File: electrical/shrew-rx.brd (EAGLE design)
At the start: 14 x 14 mm, 28 parts, among them U1 ESP32-PICO-D4, U2 SX1280IMLTRT, Y1 52MHz TCXO

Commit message: wip for rx
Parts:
- C12: value 470n -> DNP
- C17: value 100n -> 470n
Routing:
- net GND: track 27.7 -> 35.9 mm

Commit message: rx mfg file trial run
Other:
- board size 14 x 14 mm -> 15.5 x 15 mm
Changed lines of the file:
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@@
 <setting verticaltext="up"/>
 </settings>
-<grid distance="0.1" unitdist="mm" unit="mm" style="dots" multiple="10" display="no" altdistance="0.01" altunitdist="mm" altunit="mm"/>
+<grid distance="0.1" unitdist="mm" unit="mm" style="dots" multiple="10" display="yes" altdistance="0.01" altunitdist="mm" altunit="mm"/>
 <layers>
 <layer number="1" name="Top" color="4" fill="1" visible="yes" active="yes"/>
@@
 <layer number="21" name="tPlace" color="7" fill="1" visible="yes" active="yes"/>
 <layer number="22" name="bPlace" color="7" fill="1" visible="yes" active="yes"/>
-<layer number="23" name="tOrigins" color="15" fill="1" visible="yes" active="yes"/>
-<layer number="24" name="bOrigins" color="15" fill="1" visible="yes" active="yes"/>
+<layer number="23" name="tOrigins" color="15" fill="1" visible="no" active="yes"/>
+<layer number="24" name="bOrigins" color="15" fill="1" visible="no" active="yes"/>
 <layer number="25" name="tNames" color="7" fill="1" visible="no" active="yes"/>
 <layer number="26" name="bNames" color="7" fill="1" visible="no" active="yes"/>
@@
 <board>
 <plain>
-<wire x1="0" y1="0" x2="14" y2="0" width="0" layer="20"/>
-<wire x1="14" y1="0" x2="14" y2="14" width="0" layer="20"/>
-<wire x1="14" y1="14" x2="0" y2="14" width="0" layer="20"/>
-<wire x1="0" y1="14" x2="0" y2="0" width="0" layer="20"/>
-<rectangle x1="14.9" y1="7.5" x2="17.9" y2="10.5" layer="29"/>
+<wire x1="-1.5" y1="-1" x2="14" y2="-1" width="0" layer="20"/>
+<wire x1="14" y1="-1" x2="14" y2="14" width="0" layer="20"/>
+<wire x1="14" y1="14" x2="-1.5" y2="14" width="0" layer="20"/>
+<wire x1="-1.5" y1="14" x2="-1.5" y2="-1" width="0" layer="20"/>
 <rectangle x1="9.6" y1="12.1" x2="11.4" y2="13.8" layer="41"/>
 <rectangle x1="8.8" y1="12.1" x2="12.4" y2="13.8" layer="43"/>
@@
 <rectangle x1="11.4" y1="12.1" x2="13.8" y2="13.8" layer="41"/>
 <rectangle x1="12.4" y1="12.1" x2="13.8" y2="13.8" layer="43"/>
+<wire x1="-0.2" y1="14" x2="-0.2" y2="-0.2" width="0" layer="41"/>
+<wire x1="-0.2" y1="-0.2" x2="14" y2="-0.2" width="0" layer="41"/>
+<wire x1="-0.2" y1="14" x2="-0.2" y2="-0.2" width="0" layer="42"/>
+<wire x1="-0.2" y1="-0.2" x2="14" y2="-0.2" width="0" layer="42"/>
+<wire x1="-0.2" y1="14" x2="-0.2" y2="-0.2" width="0" layer="43"/>
+<wire x1="-0.2" y1="-0.2" x2="14" y2="-0.2" width="0" layer="43"/>
+<wire x1="6.6" y1="11.3" x2="6.6" y2="11.1" width="0" layer="42"/>
+<wire x1="4.8" y1="8.1" x2="4.8" y2="8" width="0" layer="41"/>
+<wire x1="1.7" y1="0.3" x2="10.3" y2="0.3" width="0" layer="41"/>
+<wire x1="0.3" y1="2.3" x2="0.3" y2="8.8" width="0" layer="41"/>
+<wire x1="8.9" y1="6" x2="9.1" y2="6" width="0" layer="41"/>
+<wire x1="10.2" y1="6" x2="10.3" y2="6" width="0" layer="41"/>
+<wire x1="7.3" y1="5.3" x2="7.8" y2="5.3" width="0" layer="41"/>
+<wire x1="7.5" y1="0.8" x2="8.4" y2="0.8" width="0" layer="42"/>
 </plain>
 <attributes>
@@
 <wire x1="9.66" y1="5.75" x2="9.66" y2="4.63" width="0.254" layer="16"/>
 <via x="12.78" y="5.67" extent="1-16" drill="0.3" shape="octagon"/>
-<polygon width="0.254" layer="2" spacing="0.1524" isolate="0.1524" thermals="no">
+<polygon width="0.254" layer="2" spacing="0.1524" isolate="0.2032" thermals="no">
 <vertex x="0" y="0"/>
 <vertex x="0" y="14"/>
@@
 <vertex x="0" y="14"/>
 <vertex x="0" y="9.5"/>
-<vertex x="1.4" y="9.5"/>
-<vertex x="1.4" y="14"/>
+<vertex x="1.3" y="9.5"/>
+<vertex x="1.3" y="14"/>
 </polygon>
 <polygon width="0.1524" layer="16" spacing="0.1524" isolate="0.1524" thermals="no">
@@
 <wire x1="3.15" y1="4.25" x2="3.15" y2="4.1" width="0.254" layer="16"/>
 <wire x1="8.35" y1="5.6" x2="8.35" y2="3.3" width="0.4064" layer="1"/>
-<polygon width="0.1524" layer="15" spacing="0.1524" isolate="0.1524" thermals="no">
+<polygon width="0.2032" layer="15" spacing="0.1524" isolate="0.2032" thermals="no">
 <vertex x="0" y="0"/>
 <vertex x="0" y="14"/>
@@
 <wire x1="9.7685" y1="10.25" x2="10.05" y2="10.25" width="0.1524" layer="1"/>
 <wire x1="10.05" y1="10.25" x2="10.1" y2="10.3" width="0.1524" layer="1"/>
-<wire x1="10.1" y1="10.3" x2="11.39" y2="10.3" width="0.1524" layer="1"/>
-<wire x1="11.39" y1="10.3" x2="11.6" y2="10.51" width="0.1524" layer="1"/>
+<wire x1="10.1" y1="10.3" x2="10.79" y2="10.3" width="0.1524" layer="1"/>
+<wire x1="10.79" y1="10.3" x2="11" y2="10.5" width="0.1524" layer="1"/>
+<wire x1="11" y1="10.5" x2="11.59" y2="10.5" width="0.1524" layer="1"/>
+<wire x1="11.59" y1="10.5" x2="11.6" y2="10.51" width="0.1524" layer="1" curve="90"/>
 <contactref element="U1" pad="13"/>
 <wire x1="10.565" y1="9.75" x2="10.65" y2="9.75" width="0.1524" layer="16"/>

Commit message: schematic stitcher
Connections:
- net +24V renamed V-ADC
- net OUT1 renamed SIG4
- net OUT2 renamed SIG3
- net OUT3 renamed SIG2
- net OUT4 renamed SIG1
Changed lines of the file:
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@@
 <wire x1="11.45" y1="4.75" x2="11.4" y2="4.75" width="0.1524" layer="16"/>
-</signal>
-<signal name="+24V">
-<contactref element="R3" pad="2"/>
-<contactref element="EDGE1" pad="5"/>
-<wire x1="9" y1="0" x2="9.05" y2="0" width="0.4064" layer="16"/>
-<wire x1="9.05" y1="0" x2="9.05" y2="1.4" width="0.4064" layer="16"/>
 </signal>
 <signal name="VM">
@@
 <wire x1="2.3" y1="4.1" x2="0" y2="1.8" width="0.1524" layer="16"/>
 </signal>
-<signal name="OUT1">
-<contactref element="EDGE1" pad="1"/>
-<contactref element="U1" pad="29"/>
-<wire x1="1" y1="0" x2="2.48" y2="1.48" width="0.1524" layer="16"/>
-<wire x1="2.48" y1="1.48" x2="4.96" y2="1.48" width="0.1524" layer="16"/>
-<wire x1="8.05" y1="3.27" x2="8.05" y2="3.735" width="0.1524" layer="16"/>
-<wire x1="4.96" y1="1.48" x2="6.75" y2="3.27" width="0.1524" layer="16"/>
-<wire x1="6.75" y1="3.27" x2="8.05" y2="3.27" width="0.1524" layer="16"/>
-</signal>
-<signal name="OUT2">
+<signal name="SIG3">
 <contactref element="EDGE1" pad="2"/>
 <contactref element="U1" pad="28"/>
@@
 <wire x1="8.18" y1="2.9" x2="8.55" y2="3.27" width="0.1524" layer="16"/>
 </signal>
-<signal name="OUT3">
+<signal name="SIG2">
 <contactref element="EDGE1" pad="3"/>
 <contactref element="U1" pad="27"/>
@@
 <wire x1="9.05" y1="3.15" x2="9.05" y2="3.735" width="0.1524" layer="16"/>
 </signal>
-<signal name="OUT4">
+<signal name="SIG1">
 <contactref element="EDGE1" pad="4"/>
 <contactref element="U1" pad="25"/>
@@
 <wire x1="7" y1="1.517884375" x2="7" y2="0" width="0.1524" layer="16"/>
 </signal>
+<signal name="SIG4">
+<contactref element="U1" pad="29"/>
+<contactref element="EDGE1" pad="1"/>
+<wire x1="1" y1="0" x2="2.48" y2="1.48" width="0.1524" layer="16"/>
+<wire x1="2.48" y1="1.48" x2="4.96" y2="1.48" width="0.1524" layer="16"/>
+<wire x1="4.96" y1="1.48" x2="6.75" y2="3.27" width="0.1524" layer="16"/>
+<wire x1="6.75" y1="3.27" x2="7.96" y2="3.27" width="0.1524" layer="16"/>
+<wire x1="7.96" y1="3.27" x2="8.05" y2="3.36" width="0.1524" layer="16"/>
+<wire x1="8.05" y1="3.36" x2="8.05" y2="3.735" width="0.1524" layer="16"/>
+</signal>
+<signal name="V-ADC">
+<contactref element="EDGE1" pad="5"/>
+<contactref element="R3" pad="2"/>
+<wire x1="9.05" y1="0" x2="9.05" y2="1.4" width="0.4064" layer="16"/>
+<wire x1="9.05" y1="0" x2="9" y2="0" width="0.4064" layer="16"/>
+</signal>
 </signals>

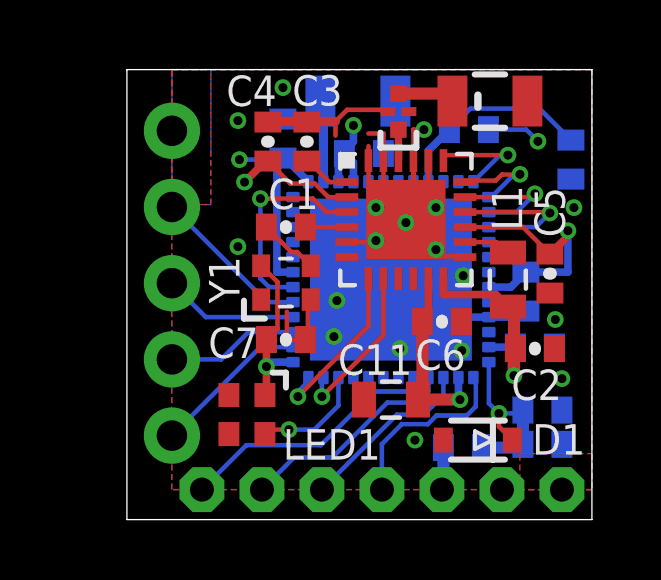
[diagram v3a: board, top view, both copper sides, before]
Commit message: changed all 0402 footprints on rx
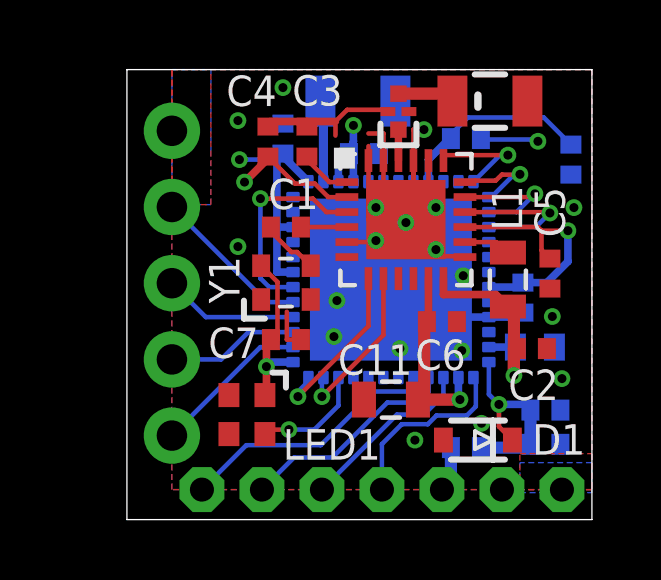
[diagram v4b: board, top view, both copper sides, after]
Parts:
- C1, C10, C13, C17, C2, C3, C4, C5, C6, C7, C8, C9: device shrew-common:0402-CAP -> shrew-common:0402-REV
- R1, R2, R3: device shrew-common:0402-RES -> shrew-common:0402-REV
- moved R1 0.32 mm to (9.80, 11.7)
- moved C9 0.22 mm to (11.7, 6.40)
- moved R3 0.10 mm to (9.80, 1.40)
- moved C17 0.10 mm to (12.4, 2.65)
- moved C2 0.10 mm to (12.0, 4.70)
- moved R2 0.10 mm to (12.4, 1.51)
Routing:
- net GND: track 35.9 -> 33.5 mm, vias 18 -> 19
- net 3.3V: track 33.2 -> 34.0 mm
- net BATT-ADC: track 6.36 -> 6.98 mm

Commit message: initial work on integrated versions
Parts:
- moved C9 0.81 mm to (11.5, 7.18), turned to 90 degrees
- moved C5 0.50 mm to (13.1, 7.20)
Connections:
- new net N$5: U1.17
- new net N$8: U1.22
- net SIG1: now also U1.20; no longer U1.25
- net SIG2: now also U1.16; no longer U1.27
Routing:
- net SIG2: track 5.94 -> 14.5 mm, vias 0 -> 2
- net GND: track 33.5 -> 39.2 mm, vias 19 -> 21
- net RADIO-RST: track 6.93 -> 12.2 mm, vias 1 -> 2
- net SIG1: track 6.21 -> 11.0 mm, vias 0 -> 2
- net 3.3V: track 34.0 -> 34.5 mm
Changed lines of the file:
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@@
 <layer number="21" name="tPlace" color="7" fill="1" visible="yes" active="yes"/>
 <layer number="22" name="bPlace" color="7" fill="1" visible="yes" active="yes"/>
-<layer number="23" name="tOrigins" color="15" fill="1" visible="no" active="yes"/>
-<layer number="24" name="bOrigins" color="15" fill="1" visible="no" active="yes"/>
+<layer number="23" name="tOrigins" color="15" fill="1" visible="yes" active="yes"/>
+<layer number="24" name="bOrigins" color="15" fill="1" visible="yes" active="yes"/>
 <layer number="25" name="tNames" color="7" fill="1" visible="no" active="yes"/>
 <layer number="26" name="bNames" color="7" fill="1" visible="no" active="yes"/>
@@
 <attribute name="VALUE" x="2.057" y="12.6795" size="0.8128" layer="27" font="vector" rot="R270"/>
 </element>
-<element name="C5" library="shrew-common" package="0402-REV" value="100n" x="12.6" y="7.2" smashed="yes" rot="R90">
-<attribute name="NAME" x="13.1015" y="8.411" size="1.016" layer="25" font="vector" rot="R90"/>
-<attribute name="VALUE" x="13.743" y="6.1205" size="0.8128" layer="27" font="vector" rot="R90"/>
+<element name="C5" library="shrew-common" package="0402-REV" value="100n" x="13.1" y="7.2" smashed="yes" rot="R90">
+<attribute name="NAME" x="13.6015" y="8.411" size="1.016" layer="25" font="vector" rot="R90"/>
+<attribute name="VALUE" x="14.243" y="6.1205" size="0.8128" layer="27" font="vector" rot="R90"/>
 </element>
 <element name="C6" library="shrew-common" package="0402-REV" value="100n" x="9" y="5.6" smashed="yes" rot="R180">
@@
 <attribute name="VALUE" x="5.3205" y="12.343" size="0.4064" layer="28" rot="MR180"/>
 </element>
-<element name="C9" library="shrew-common" package="0402-REV" value="100n" x="11.7" y="6.4" smashed="yes" rot="MR270">
-<attribute name="NAME" x="11.0015" y="7.289" size="0.4064" layer="26" rot="MR270"/>
-<attribute name="VALUE" x="12.843" y="7.4795" size="0.4064" layer="28" rot="MR270"/>
+<element name="C9" library="shrew-common" package="0402-REV" value="100n" x="11.48" y="7.18" smashed="yes" rot="MR90">
+<attribute name="NAME" x="12.1785" y="6.291" size="0.4064" layer="26" rot="MR90"/>
+<attribute name="VALUE" x="10.337" y="6.1005" size="0.4064" layer="28" rot="MR90"/>
 </element>
 <element name="LED1" library="shrew-core" package="SK6812-EC20" value="SK6812-EC20" x="2.5" y="2.5" smashed="yes" rot="R90">
@@
 <via x="9.71" y="7.13" extent="1-16" drill="0.3" shape="octagon"/>
 <via x="9.66" y="4.63" extent="1-16" drill="0.3" shape="octagon"/>
-<wire x1="10.565" y1="5.75" x2="11.6" y2="5.75" width="0.254" layer="16"/>
-<wire x1="11.6" y1="5.75" x2="11.7" y2="5.9" width="0.254" layer="16"/>
 <wire x1="10.565" y1="5.75" x2="9.66" y2="5.75" width="0.254" layer="16"/>
 <wire x1="9.66" y1="5.75" x2="9.66" y2="4.63" width="0.254" layer="16"/>
-<via x="12.68" y="5.77" extent="1-16" drill="0.3" shape="octagon"/>
+<via x="13.38" y="5.77" extent="1-16" drill="0.3" shape="octagon"/>
 <polygon width="0.254" layer="2" spacing="0.1524" isolate="0.2032" thermals="no">
 <vertex x="0" y="0"/>
@@
 <contactref element="FL1" pad="2"/>
 <contactref element="FL1" pad="4"/>
+<via x="12.3" y="7.38" extent="1-16" drill="0.3" shape="octagon"/>
+<wire x1="11.48" y1="7.68" x2="11.65" y2="7.51" width="0.254" layer="16"/>
+<wire x1="11.65" y1="7.51" x2="12.3" y2="7.51" width="0.254" layer="16"/>
+<wire x1="12.3" y1="7.51" x2="12.3" y2="7.38" width="0.254" layer="16"/>
+<wire x1="9.66" y1="4.62" x2="10.32" y2="3.96" width="0.1524" layer="15"/>
+<wire x1="10.32" y1="3.96" x2="10.32" y2="2.21" width="0.1524" layer="15"/>
+<wire x1="8.1" y1="1.65" x2="8.1" y2="4.2" width="0.1524" layer="15"/>
+<wire x1="8.1" y1="4.2" x2="7.61" y2="4.69" width="0.1524" layer="15"/>
+<via x="1.5" y="9.2" extent="1-16" drill="0.3" shape="octagon"/>
 </signal>
 <signal name="VDD_SDIO">
@@
 <wire x1="3.5" y1="7.25" x2="3.5" y2="8.75" width="0.254" layer="16"/>
 <wire x1="4.035" y1="4.25" x2="3.15" y2="4.25" width="0.254" layer="16"/>
-<wire x1="13.2" y1="7.6" x2="13.2" y2="8.63" width="0.254" layer="16"/>
+<wire x1="13.2" y1="8.63" x2="13.2" y2="6.79" width="0.254" layer="16"/>
+<wire x1="13.2" y1="6.79" x2="11.48" y2="6.79" width="0.254" layer="16"/>
 <via x="13.2" y="8.63" extent="1-16" drill="0.3" shape="octagon"/>
-<wire x1="10.565" y1="6.75" x2="11.7" y2="6.75" width="0.254" layer="16"/>
 <wire x1="8.55" y1="7.0315" x2="8.55" y2="5.9" width="0.254" layer="1"/>
 <wire x1="8.55" y1="5.9" x2="8.5" y2="5.6" width="0.254" layer="1"/>
@@
 <wire x1="13.2" y1="8.63" x2="12.32" y2="8.63" width="0.1524" layer="1"/>
 <wire x1="12.32" y1="8.63" x2="12.2" y2="8.75" width="0.1524" layer="1"/>
-<wire x1="12.6" y1="7.7" x2="12.32" y2="7.98" width="0.1524" layer="1"/>
-<wire x1="12.32" y1="7.98" x2="12.32" y2="8.63" width="0.1524" layer="1"/>
 <wire x1="8.5" y1="5.6" x2="8.41" y2="5.51" width="0.4064" layer="1"/>
 <wire x1="8.41" y1="5.51" x2="8.41" y2="3" width="0.4064" layer="1"/>
@@
 <wire x1="12.14" y1="11.67" x2="10.3" y2="11.67" width="0.1524" layer="16"/>
 <wire x1="10.3" y1="11.67" x2="10.3" y2="11.7" width="0.1524" layer="16"/>
-<wire x1="11.7" y1="6.75" x2="11.7" y2="6.9" width="0.254" layer="16"/>
-<wire x1="13.2" y1="7.6" x2="12.5" y2="6.9" width="0.254" layer="16"/>
-<wire x1="12.5" y1="6.9" x2="11.7" y2="6.9" width="0.254" layer="16"/>
+<wire x1="13.1" y1="7.7" x2="13.2" y2="7.7" width="0.254" layer="1"/>
+<wire x1="13.2" y1="7.7" x2="13.2" y2="8.63" width="0.254" layer="1"/>
+<wire x1="10.565" y1="6.75" x2="11.48" y2="6.75" width="0.254" layer="16"/>
+<wire x1="11.48" y1="6.75" x2="11.48" y2="6.68" width="0.254" layer="16"/>
+<wire x1="11.48" y1="6.79" x2="11.48" y2="6.68" width="0.254" layer="16"/>
 </signal>
 <signal name="U0TXD">
@@
 <wire x1="3.241546875" y1="6.75" x2="2.95" y2="7.041546875" width="0.1524" layer="16"/>
 <wire x1="2.95" y1="7.041546875" x2="2.95" y2="9.7" width="0.1524" layer="16"/>
+<via x="1.4" y="5.1" extent="1-16" drill="0.3" shape="octagon"/>
+<wire x1="1.4" y1="5.1" x2="1.4" y2="8.15" width="0.1524" layer="1"/>
+<wire x1="1.4" y1="8.15" x2="2.95" y2="9.7" width="0.1524" layer="1"/>
 </signal>
 <signal name="RADIO-BUSY">
@@
 <signal name="SIG2">
 <contactref element="EDGE1" pad="3"/>
-<contactref element="U1" pad="27"/>
-<wire x1="5" y1="0" x2="7.5" y2="2.5" width="0.1524" layer="16"/>
-<wire x1="7.5" y1="2.5" x2="8.4" y2="2.5" width="0.1524" layer="16"/>
-<wire x1="8.4" y1="2.5" x2="9.05" y2="3.15" width="0.1524" layer="16"/>
-<wire x1="9.05" y1="3.15" x2="9.05" y2="3.735" width="0.1524" layer="16"/>
+<contactref element="U1" pad="16"/>
+<via x="12.3" y="8.1" extent="1-16" drill="0.3" shape="octagon"/>
+<wire x1="10.565" y1="8.25" x2="12.15" y2="8.25" width="0.1524" layer="16"/>
+<wire x1="12.15" y1="8.25" x2="12.3" y2="8.1" width="0.1524" layer="16"/>
+<via x="6" y="0.9" extent="1-16" drill="0.3" shape="octagon"/>
+<wire x1="6" y1="0.9" x2="6" y2="1.5" width="0.1524" layer="2"/>
+<wire x1="6" y1="1.5" x2="8.5" y2="4" width="0.1524" layer="2"/>
+<wire x1="8.5" y1="4" x2="10.06" y2="4" width="0.1524" layer="2"/>
+<wire x1="10.06" y1="4" x2="10.86" y2="4.8" width="0.1524" layer="2"/>
+<wire x1="10.86" y1="4.8" x2="10.86" y2="7.64656875" width="0.1524" layer="2"/>
+<wire x1="10.86" y1="7.64656875" x2="11.31343125" y2="8.1" width="0.1524" layer="2"/>
+<wire x1="11.31343125" y1="8.1" x2="12.3" y2="8.1" width="0.1524" layer="2"/>
+<wire x1="6" y1="0.9" x2="5.9" y2="0.9" width="0.1524" layer="16"/>
+<wire x1="5.9" y1="0.9" x2="5" y2="0" width="0.1524" layer="16"/>
 </signal>
 <signal name="SIG1">
 <contactref element="EDGE1" pad="4"/>
-<contactref element="U1" pad="25"/>
-<wire x1="10.05" y1="3.735" x2="10.13" y2="3.735" width="0.1524" layer="16"/>
-<wire x1="10.13" y1="3.735" x2="10.13" y2="2.77" width="0.1524" layer="16"/>
-<wire x1="10.13" y1="2.77" x2="9.83" y2="2.47" width="0.1524" layer="16"/>
-<wire x1="9.83" y1="2.47" x2="8.82" y2="2.47" width="0.1524" layer="16"/>
-<wire x1="8.82" y1="2.47" x2="8.53" y2="2.18" width="0.1524" layer="16"/>
-<wire x1="8.53" y1="2.18" x2="7.662115625" y2="2.18" width="0.1524" layer="16"/>
-<wire x1="7.662115625" y1="2.18" x2="7" y2="1.517884375" width="0.1524" layer="16"/>
-<wire x1="7" y1="1.517884375" x2="7" y2="0" width="0.1524" layer="16"/>
+<contactref element="U1" pad="20"/>
+<via x="12.3" y="5.9" extent="1-16" drill="0.3" shape="octagon"/>
+<wire x1="11.23" y1="5.9" x2="12.3" y2="5.9" width="0.1524" layer="16"/>
+<wire x1="11.23" y1="5.9" x2="10.96" y2="6.16" width="0.1524" layer="16"/>
+<wire x1="10.96" y1="6.16" x2="10.565" y2="6.16" width="0.1524" layer="16"/>
+<wire x1="10.565" y1="6.16" x2="10.565" y2="6.25" width="0.1524" layer="16"/>
+<via x="7.2" y="1.4" extent="1-16" drill="0.3" shape="octagon"/>
+<wire x1="7.2" y1="1.4" x2="7.2" y2="2.1" width="0.1524" layer="2"/>
+<wire x1="7.2" y1="2.1" x2="8.7" y2="3.6" width="0.1524" layer="2"/>
+<wire x1="8.7" y1="3.6" x2="10.3" y2="3.6" width="0.1524" layer="2"/>
+<wire x1="10.3" y1="3.6" x2="11.9" y2="5.2" width="0.1524" layer="2"/>
+<wire x1="11.9" y1="5.2" x2="11.9" y2="5.5" width="0.1524" layer="2"/>
+<wire x1="11.9" y1="5.5" x2="12.3" y2="5.9" width="0.1524" layer="2"/>
+<wire x1="7.2" y1="1.4" x2="7.2" y2="0.2" width="0.1524" layer="16"/>
+<wire x1="7.2" y1="0.2" x2="7" y2="0" width="0.1524" layer="16"/>
 </signal>
 <signal name="SIG4">
@@
 <wire x1="9.3" y1="0" x2="9.3" y2="1.4" width="0.4064" layer="16"/>
 </signal>
+<signal name="N$5">
+<contactref element="U1" pad="17"/>
+</signal>
+<signal name="N$8">
+<contactref element="U1" pad="22"/>
+</signal>
 </signals>
